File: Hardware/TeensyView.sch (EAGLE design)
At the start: 23 parts, among them J1 DNP, J2 DNP

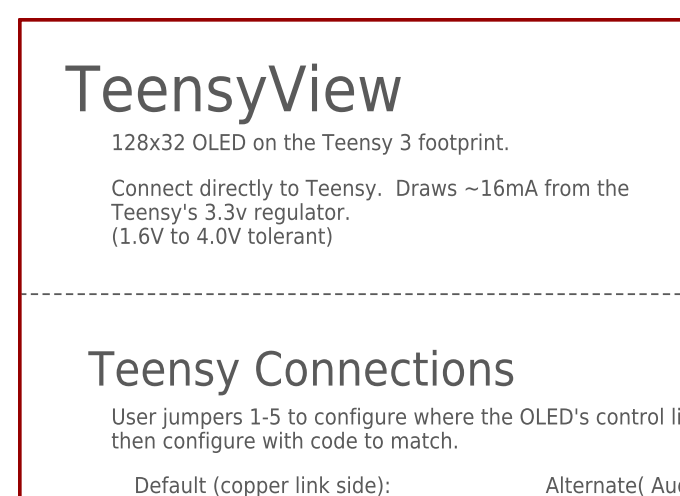
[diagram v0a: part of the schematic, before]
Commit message: Made silk and version number changes for reds
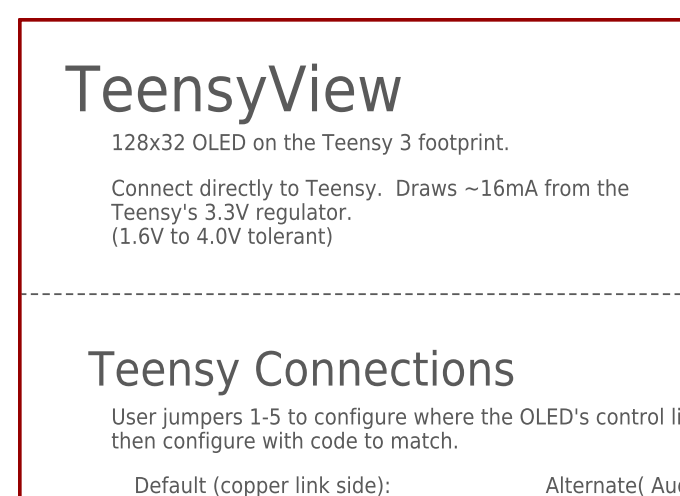
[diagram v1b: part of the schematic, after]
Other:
- note added: "Connect directly to Teensy. Draws ~16mA from the Teensy's 3.3V regulator. (1.6V to 4.0V tolerant)"
- note removed: "Connect directly to Teensy. Draws ~16mA from the Teensy's 3.3v regulator. (1.6V to 4.0V tolerant)"
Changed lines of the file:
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@@
 <text x="5.08" y="175.26" size="5.08" layer="97" font="vector">TeensyView</text>
 <text x="10.16" y="167.64" size="1.778" layer="97" font="vector" align="top-left">Connect directly to Teensy.  Draws ~16mA from the
-Teensy's 3.3v regulator.
+Teensy's 3.3V regulator.
 (1.6V to 4.0V tolerant)</text>
 <text x="35.56" y="48.26" size="1.778" layer="97" font="vector" rot="MR180" align="center">7</text>
